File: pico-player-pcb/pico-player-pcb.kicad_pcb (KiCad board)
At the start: 2 copper layers, 56.9 x 66 mm, 23 parts, among them J1 AudioPlug3, U1 Pico, U2 SN76489, U3 SN76489

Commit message: minor pcb tweak
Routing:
- net Net-(U1-Pad6): track 30.2 -> 32.9 mm
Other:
- board size 56.9 x 66 mm -> 57.9 x 67.1 mm
- board text added: "Raspberry Pi Pico"
- board text added: "SN76489"

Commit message: protip: draw your traces and then don't look at them again
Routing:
- net Net-(U1-Pad7): track 25.7 -> 21.7 mm
- net Net-(D6-Pad2): track 18.3 -> 20.7 mm
- net Net-(D7-Pad2): track 14.1 -> 12.3 mm

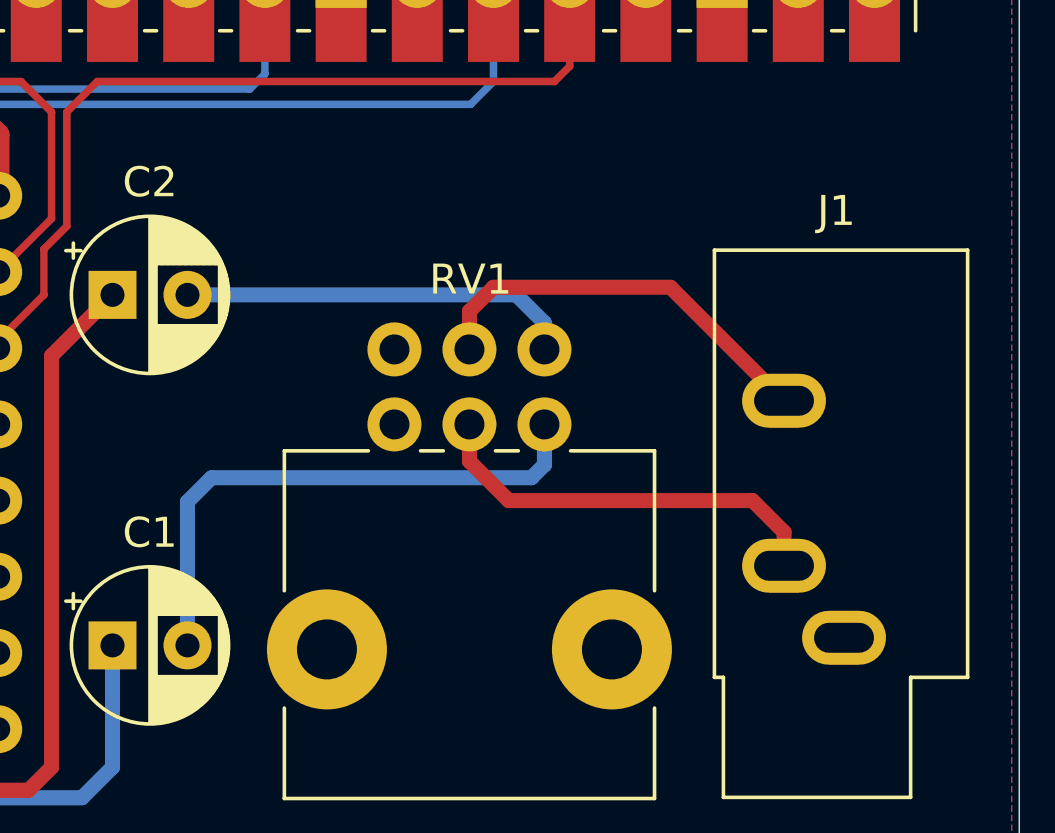
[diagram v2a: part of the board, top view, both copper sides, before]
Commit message: I think probably the pot was wired backward
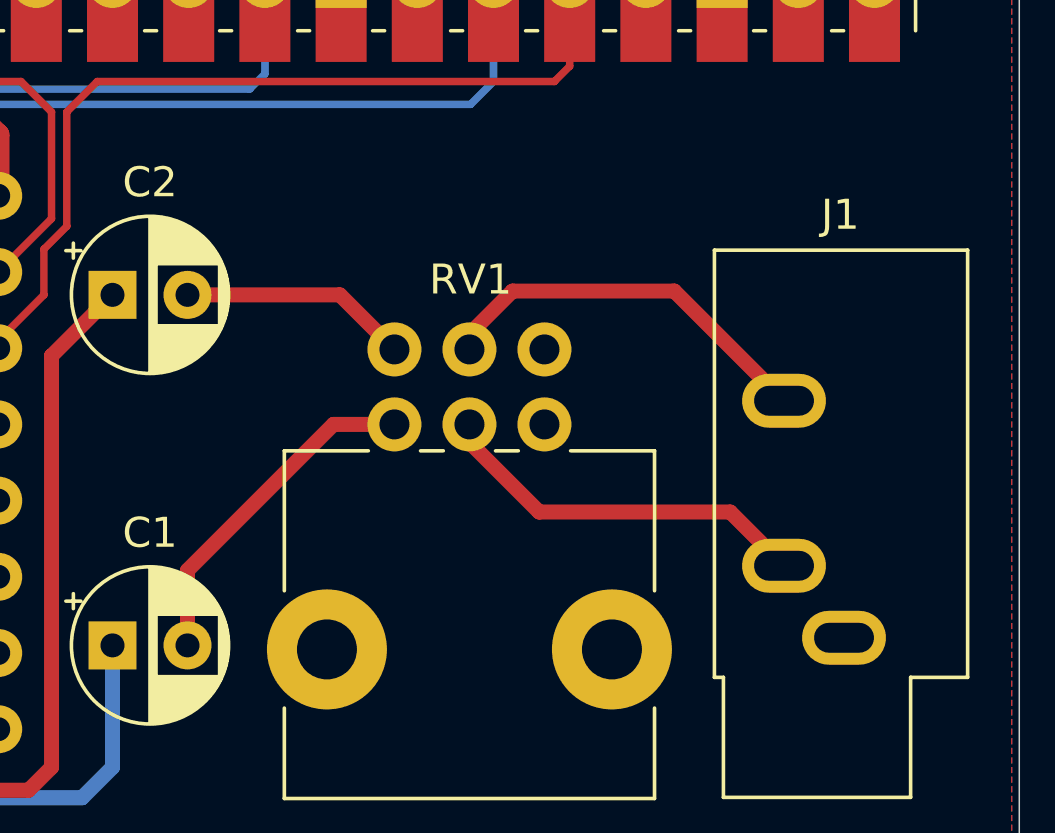
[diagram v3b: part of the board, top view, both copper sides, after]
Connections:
- RV1 pad 1: GND -> Net-(C1-Pad2)
- RV1 pad 3: Net-(C1-Pad2) -> GND
- RV1 pad 4: GND -> Net-(C2-Pad2)
- RV1 pad 6: Net-(C2-Pad2) -> GND
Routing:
- net Net-(C1-Pad2): track 18.5 -> 11.4 mm
- net Net-(C2-Pad2): track 13.2 -> 7.65 mm
- net Net-(J1-PadT): track 13.8 -> 12.8 mm
- net Net-(J1-PadR): track 13.7 -> 13.1 mm

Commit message: ... sigh, it was better before
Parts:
- moved RV1 9.22 mm to (150.7, 124.3), turned to 90 degrees
- moved R2 2.22 mm to (121.8, 70.2), turned to 180 degrees
- moved R4 2.22 mm to (135.0, 70.2), turned to 180 degrees
- moved R5 2.22 mm to (141.6, 70.2), turned to 180 degrees
- moved R6 2.22 mm to (148.2, 70.2), turned to 180 degrees
- moved R7 2.22 mm to (154.8, 70.2), turned to 180 degrees
- moved R8 2.22 mm to (161.4, 70.2), turned to 180 degrees
- moved R1 2.22 mm to (115.2, 70.2), turned to 180 degrees
- moved R3 2.22 mm to (128.4, 70.2), turned to 180 degrees
- moved LED1 1.98 mm to (112.6, 75.8), turned to 0 degrees
- moved LED2 1.98 mm to (119.3, 75.8), turned to 0 degrees
- moved LED3 1.98 mm to (125.9, 75.8), turned to 0 degrees
- moved LED4 1.98 mm to (132.5, 75.8), turned to 0 degrees
- moved LED5 1.98 mm to (139.1, 75.8), turned to 0 degrees
- moved LED6 1.98 mm to (145.7, 75.8), turned to 0 degrees
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- renumbered D1 to LED1, D2 to LED2, D3 to LED3, D4 to LED4, D5 to LED5, D6 to LED6, D7 to LED7, D8 to LED8
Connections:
- net Net-(D1-Pad2) renamed /led1
- net Net-(D2-Pad2) renamed /led2
- net Net-(D3-Pad2) renamed /led3
- net Net-(D4-Pad2) renamed /led4
- net Net-(D5-Pad2) renamed /led5
- net Net-(D6-Pad2) renamed /led6
- net Net-(D7-Pad2) renamed /led7
- net Net-(D8-Pad2) renamed /led8
- net Net-(U1-Pad1) renamed /d0
- net Net-(U1-Pad10) renamed /d7
- net Net-(U1-Pad11) renamed /we-1
- net Net-(U1-Pad12) renamed /we-2
- net Net-(U1-Pad14) renamed /oe-1
- net Net-(U1-Pad15) renamed /oe-2
- net Net-(U1-Pad16) renamed /clock
- net Net-(U1-Pad2) renamed /d1
- net Net-(U1-Pad4) renamed /d2
- net Net-(U1-Pad5) renamed /d3
- net Net-(U1-Pad6) renamed /d4
- net Net-(U1-Pad7) renamed /d5
- net Net-(U1-Pad9) renamed /d6
- RV1 pad 1: Net-(C1-Pad2) -> GND
- RV1 pad 3: GND -> Net-(C1-Pad2)
- RV1 pad 4: Net-(C2-Pad2) -> GND
- RV1 pad 6: GND -> Net-(C2-Pad2)
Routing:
- net Net-(C2-Pad2): track 7.65 -> 17.3 mm
- net Net-(J1-PadR): track 13.1 -> 18.1 mm
- net Net-(C1-Pad2): track 11.4 -> 7.35 mm
- net /led1: track 33.5 -> 29.5 mm
- net /led3: track 27.8 -> 24.0 mm
- net /led2: track 31.9 -> 28.2 mm
- net /led4: track 25.2 -> 21.8 mm
- net /led6: track 20.7 -> 18.3 mm
- net /led8: track 31.1 -> 28.8 mm
- net Net-(LED8-Pad1): track 3.56 -> 5.59 mm
- net Net-(LED7-Pad1): track 3.56 -> 5.59 mm
- net Net-(LED6-Pad1): track 3.56 -> 5.59 mm
- net Net-(LED5-Pad1): track 3.56 -> 5.59 mm
- net Net-(LED4-Pad1): track 3.56 -> 5.59 mm
- net Net-(LED3-Pad1): track 3.56 -> 5.59 mm
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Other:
- board size 57.9 x 67.1 mm -> 57.9 x 65.5 mm
- board text added: "pico-player v0.2 by Jeremy Stanley 2021-02"
- board text removed: "pico-player v0.1 by Jeremy Stanley 2021-02"

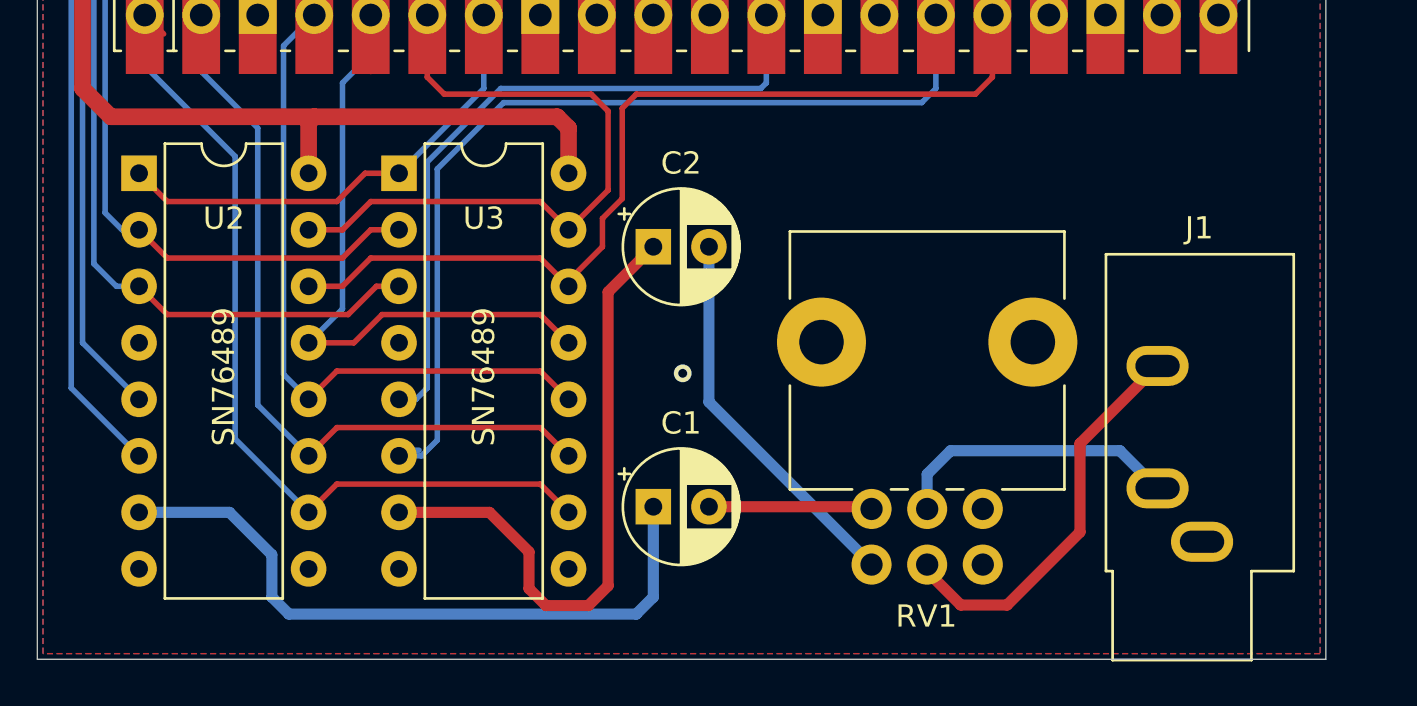
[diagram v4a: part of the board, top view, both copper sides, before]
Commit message: rearrange slightly
the potentiometer was upside-down, at least when you install
a knob with a marker

it's nice to have the audio jack on the side, so you can
stand the board up
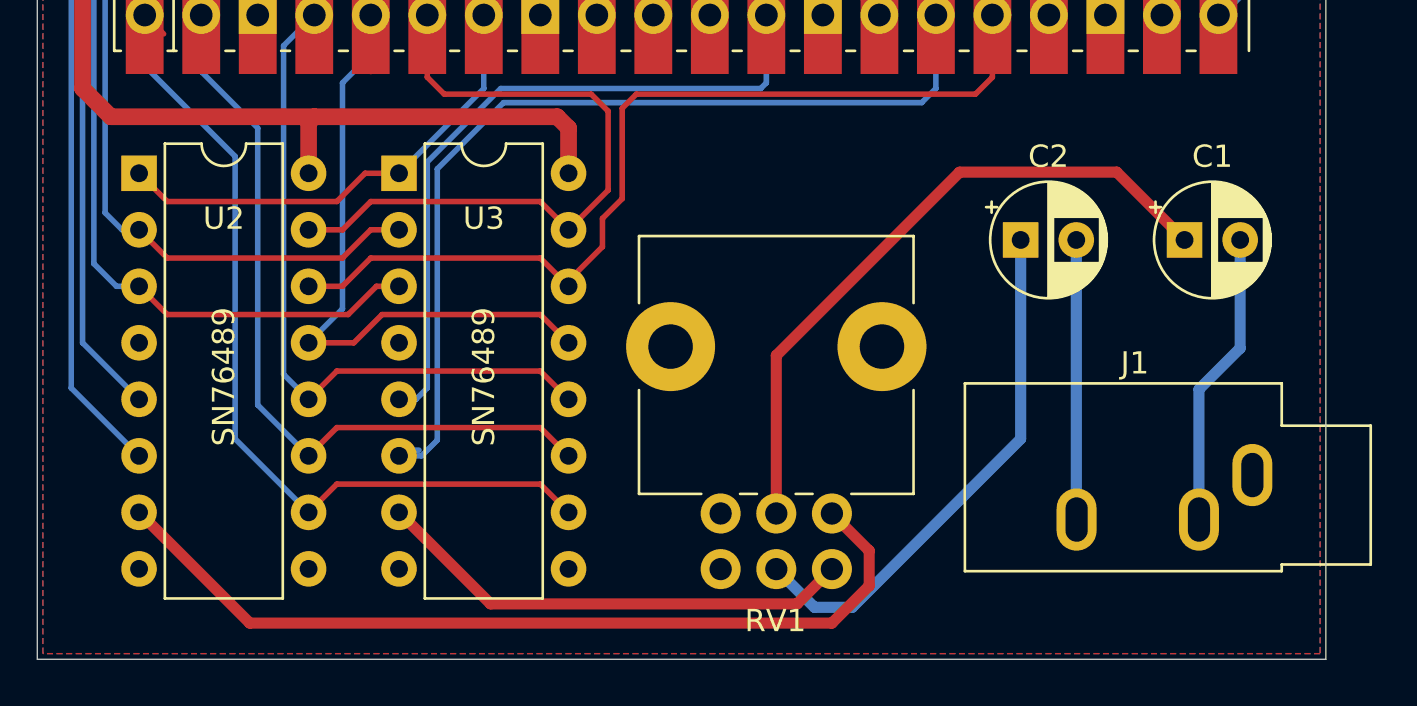
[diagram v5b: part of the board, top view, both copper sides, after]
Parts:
- J1: value AudioPlug3 -> AudioJack3
- moved C1 26.7 mm to (159.8, 112.2)
- moved C2 16.5 mm to (152.4, 112.2)
- moved RV1 6.78 mm to (143.9, 124.5)
- moved J1 3.75 mm to (162.8, 122.8), turned to 270 degrees
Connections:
- J1 pad R: Net-(J1-PadR) -> Net-(C2-Pad2)
- J1 pad T: Net-(J1-PadT) -> Net-(C1-Pad2)
- RV1 pad 1: GND -> Net-(RV1-Pad1)
- RV1 pad 2: Net-(J1-PadT) -> Net-(C1-Pad1)
- RV1 pad 3: Net-(C1-Pad2) -> GND
- RV1 pad 4: GND -> Net-(RV1-Pad4)
- RV1 pad 5: Net-(J1-PadR) -> Net-(C2-Pad1)
- RV1 pad 6: Net-(C2-Pad2) -> GND
- U2 pad 7: Net-(C1-Pad1) -> Net-(RV1-Pad1)
- U3 pad 7: Net-(C2-Pad1) -> Net-(RV1-Pad4)
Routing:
- net Net-(RV1-Pad1): track 0.00 -> 39.5 mm
- net Net-(RV1-Pad4): track 0.00 -> 21.8 mm
- net Net-(J1-PadR): track 18.1 -> 0.00 mm
- net Net-(J1-PadT): track 13.1 -> 0.00 mm
- net Net-(C1-Pad2): track 7.35 -> 13.3 mm
- net Net-(C2-Pad1): track 28.6 -> 23.8 mm
- net Net-(C2-Pad2): track 17.3 -> 12.6 mm
- net GND: vias 1 -> 0
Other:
- board text added: "pico-player v0.3 by Jeremy Stanley 2021-03"
- board text removed: "pico-player v0.2 by Jeremy Stanley 2021-02"
